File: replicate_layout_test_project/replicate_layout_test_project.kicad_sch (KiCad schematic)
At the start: 1 part, among them U101 TMS320F28027DA

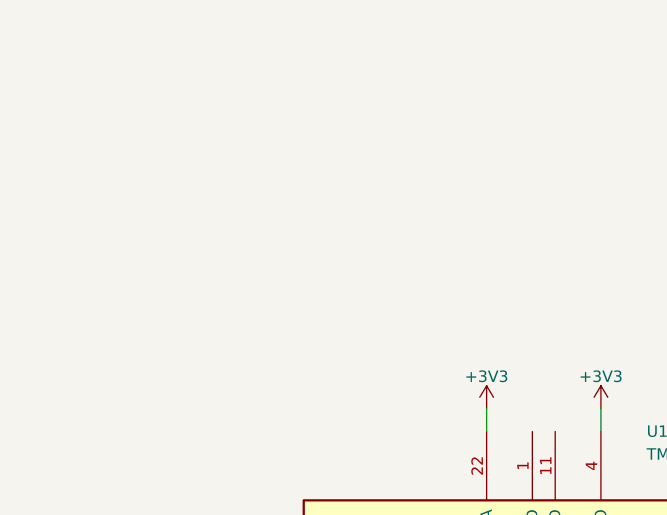
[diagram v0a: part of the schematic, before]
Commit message: Improve error messages that user sees
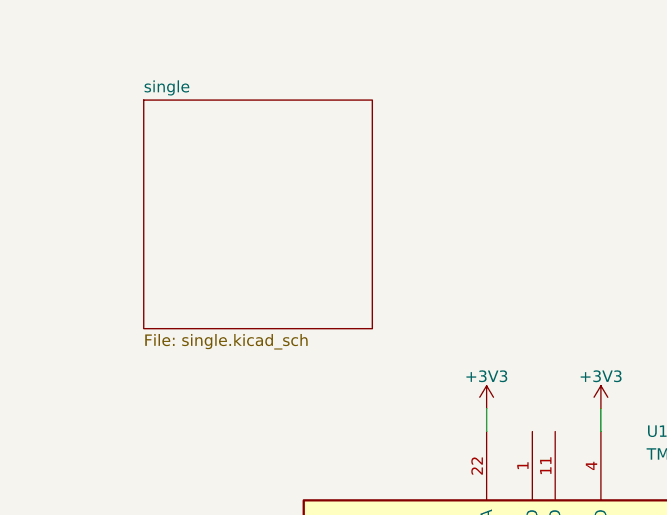
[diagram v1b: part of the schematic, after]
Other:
- added sheet single (single.kicad_sch)
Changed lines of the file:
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@@
+    )
+  )
+  (sheet (at 38.1 25.4) (size 25.4 25.4) (fields_autoplaced)
+    (stroke (width 0.1524) (type solid) (color 0 0 0 0))
+    (fill (color 0 0 0 0.0000))
+    (property "Sheet name" "single" (id 0) (at 38.1 24.6884 0)
+      (effects (font (size 1.27 1.27)) (justify left bottom))
+    )
+    (property "Sheet file" "single.kicad_sch" (id 1) (at 38.1 51.3846 0)
+      (effects (font (size 1.27 1.27)) (justify left top))
     )
   )
@@
     (path "/064636e8-22cf-4697-b1a6-7eccd3abe6c4/34cc6c9e-24b0-428f-84d8-5d06d6f728e7" (page "13"))
     (path "/7d3ced03-e1a1-476b-8e28-170d221aaf14" (page "14"))
+    (path "/4434b92d-b719-4ab5-a58e-7a9a1e1f84e7" (page "15"))
   )
   (symbol_instances
@@
       (reference "R1402") (unit 1) (value "20R") (footprint "Passives:R1206M")
     )
+    (path "/4434b92d-b719-4ab5-a58e-7a9a1e1f84e7/e5eebc7a-9eb9-4a8c-9195-f72239383f04"
+      (reference "R1501") (unit 1) (value "R1206") (footprint "Passives:R1206M")
+    )
     (path "/f19c9655-8ddb-411a-96dd-bd986870c3c6"

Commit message: updated test project
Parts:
- removed U101: TMS320F28027DA, Package_SO:TSSOP-38_4.4x9.7mm_P0.5mm, symbol ICs:TMS320F28027DA
- added C101, C102: C, Capacitor_SMD:C_1206_3216Metric, symbol Device:C
- added J101: In, Connector_PinHeader_2.54mm:PinHeader_1x02_P2.54mm_Vertical, symbol Connector_Generic:Conn_01x02
- added J102: Out, Connector_PinHeader_2.54mm:PinHeader_1x02_P2.54mm_Vertical, symbol Connector_Generic:Conn_01x02
- added R101, R102, R103, R104, R105, R106, R107, R108: R, Resistor_SMD:R_1206_3216Metric, symbol Device:R
- added U101: NE5532, Package_SO:SOIC-8_5.23x5.23mm_P1.27mm, symbol Amplifier_Operational:NE5532
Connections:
- net GND: now also J101.1 (Pin_1), J102.2 (Pin_2), U101.3 (+), U101.5 (+)
- new net: R106.2, R107.1, U101.1
- new net: C102.2, R107.2, R108.1, U101.6 (-)
- new net: R101.2, R102.2, R103.2, R104.2, R105.2, R106.1, U101.2 (-)
- new net: C102.1, J102.1 (Pin_1), R108.2, U101.7
- new net +15V: C101.1, U101.8 (V+)
- new net -15V: C101.2, U101.4 (V-)
- new net Cascade/in: J101.2 (Pin_2)
- new net Cascade/out: R101.1
- new net Cascade1/out: R102.1
- new net Cascade2/out: R103.1
- new net Cascade3/out: R104.1
- new net low_pass2/out: R105.1
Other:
- removed sheet Full Bridge
- removed sheet Full Bridge1
- removed sheet Full Bridge2
- removed sheet Leg+1
- removed sheet single
- added sheet Cascade (cascade.kicad_sch)
- added sheet Cascade1 (cascade.kicad_sch)
- added sheet Cascade2 (cascade.kicad_sch)
- added sheet Cascade3 (cascade.kicad_sch)
- added sheet low_pass2 (low_pass.kicad_sch)

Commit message: update test project
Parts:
- added R109: R, Resistor_SMD:R_1206_3216Metric, symbol Device:R
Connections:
- net at R101.2, R102.2, R103.2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: now also R109.2
- new net low_pass3/out: R109.1
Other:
- added sheet low_pass3 (low_pass.kicad_sch)
- moved on the sheet: R101, R102, R103, R104, R105
